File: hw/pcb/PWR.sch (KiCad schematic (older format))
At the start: 18 parts, among them J401 PWR, U401 R-78E3.3-1.0, U402 ADP7118

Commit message: wm8978 PCB design files
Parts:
- JP401: value Jumper_2_Open -> default open
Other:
- note added: "Bridge solder jumper if you do NOT want to use U402 (saves the expensive low noise \nLDO), however audio quality is significantly impacted by digital noise in my \nexperience. For pro audio quality U402 is mandatory!"
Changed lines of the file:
@@
 encoding utf-8
 Sheet 4 6
-Title "CTAG TBD Eurorack Audio Module"
-Date "2020-03-18"
-Rev "B"
+Title "CTAG-TBD"
+Date "2020-06-06"
+Rev "C"
 Comp "(c) Robert Manzke 2020"
 Comment1 "https://creativecommons.org/licenses/by-nc-sa/4.0/"
@@
 P 6900 2800
 F 0 "JP401" H 6900 3035 50  0000 C CNN
-F 1 "Jumper_2_Open" H 6900 2944 50  0000 C CNN
+F 1 "default open" H 6900 2944 50  0000 C CNN
 F 2 "Jumper:SolderJumper-2_P1.3mm_Open_TrianglePad1.0x1.5mm" H 6900 2800 50  0001 C CNN
 F 3 "~" H 6900 2800 50  0001 C CNN
@@
 Wire Wire Line
 	2800 2800 2800 2400
+Text Notes 6600 3250 0    50   ~ 0
+Bridge solder jumper if you do NOT want to use U402 (saves the expensive low noise \nLDO), however audio quality is significantly impacted by digital noise in my \nexperience. For pro audio quality U402 is mandatory!
 $EndSCHEMATC

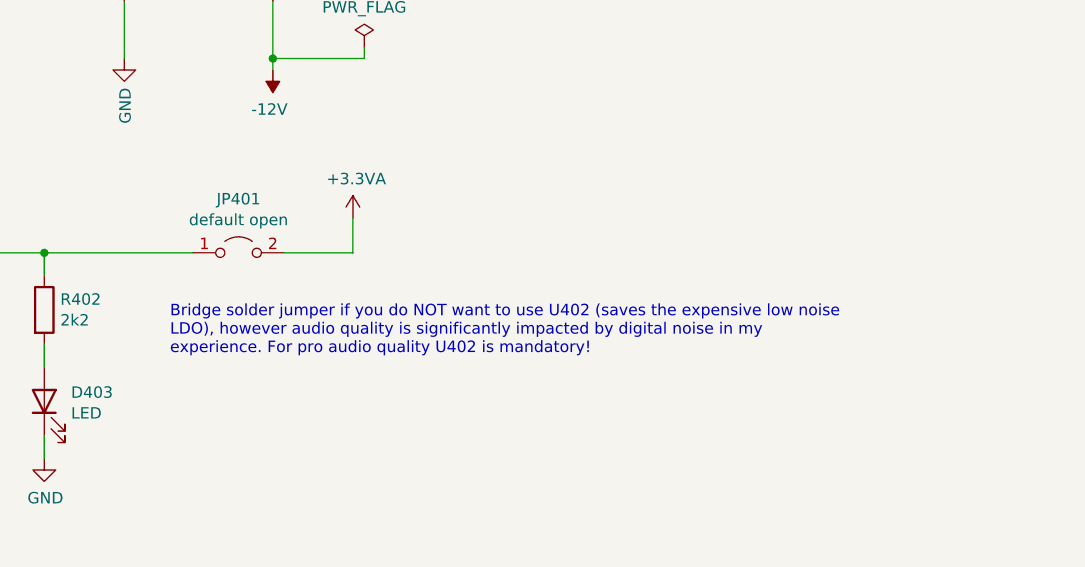
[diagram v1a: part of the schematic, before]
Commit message: fixed severe PCB issue, clearance of ground fills was too small, could lead to thermal instability
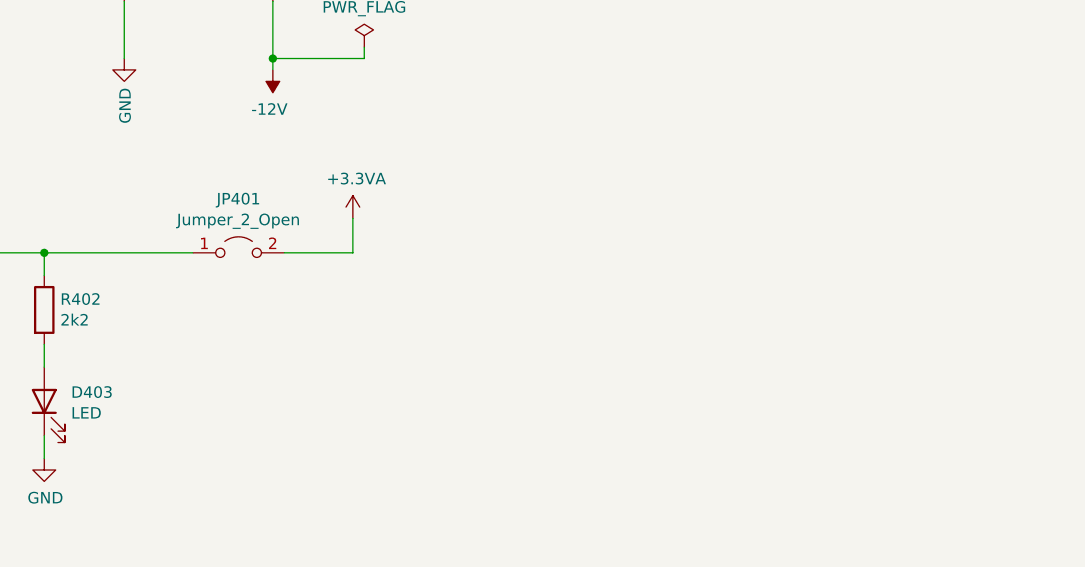
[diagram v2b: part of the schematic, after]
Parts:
- JP401: value default open -> Jumper_2_Open
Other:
- note removed: "Bridge solder jumper if you do NOT want to use U402 (saves the expensive low noise \nLDO), however audio quality is significantly impacted by digital noise in my \nexperience. For pro audio quality U402 is mandatory!"
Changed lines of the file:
@@
 encoding utf-8
 Sheet 4 6
-Title "CTAG-TBD"
-Date "2020-06-06"
-Rev "C"
+Title "ESP32 Eurorack Audio Module"
+Date "2020-08-18"
+Rev "G"
 Comp "(c) Robert Manzke 2020"
 Comment1 "https://creativecommons.org/licenses/by-nc-sa/4.0/"
@@
 P 6900 2800
 F 0 "JP401" H 6900 3035 50  0000 C CNN
-F 1 "default open" H 6900 2944 50  0000 C CNN
+F 1 "Jumper_2_Open" H 6900 2944 50  0000 C CNN
 F 2 "Jumper:SolderJumper-2_P1.3mm_Open_TrianglePad1.0x1.5mm" H 6900 2800 50  0001 C CNN
 F 3 "~" H 6900 2800 50  0001 C CNN
@@
 Wire Wire Line
 	2800 2800 2800 2400
-Text Notes 6600 3250 0    50   ~ 0
-Bridge solder jumper if you do NOT want to use U402 (saves the expensive low noise \nLDO), however audio quality is significantly impacted by digital noise in my \nexperience. For pro audio quality U402 is mandatory!
 $EndSCHEMATC

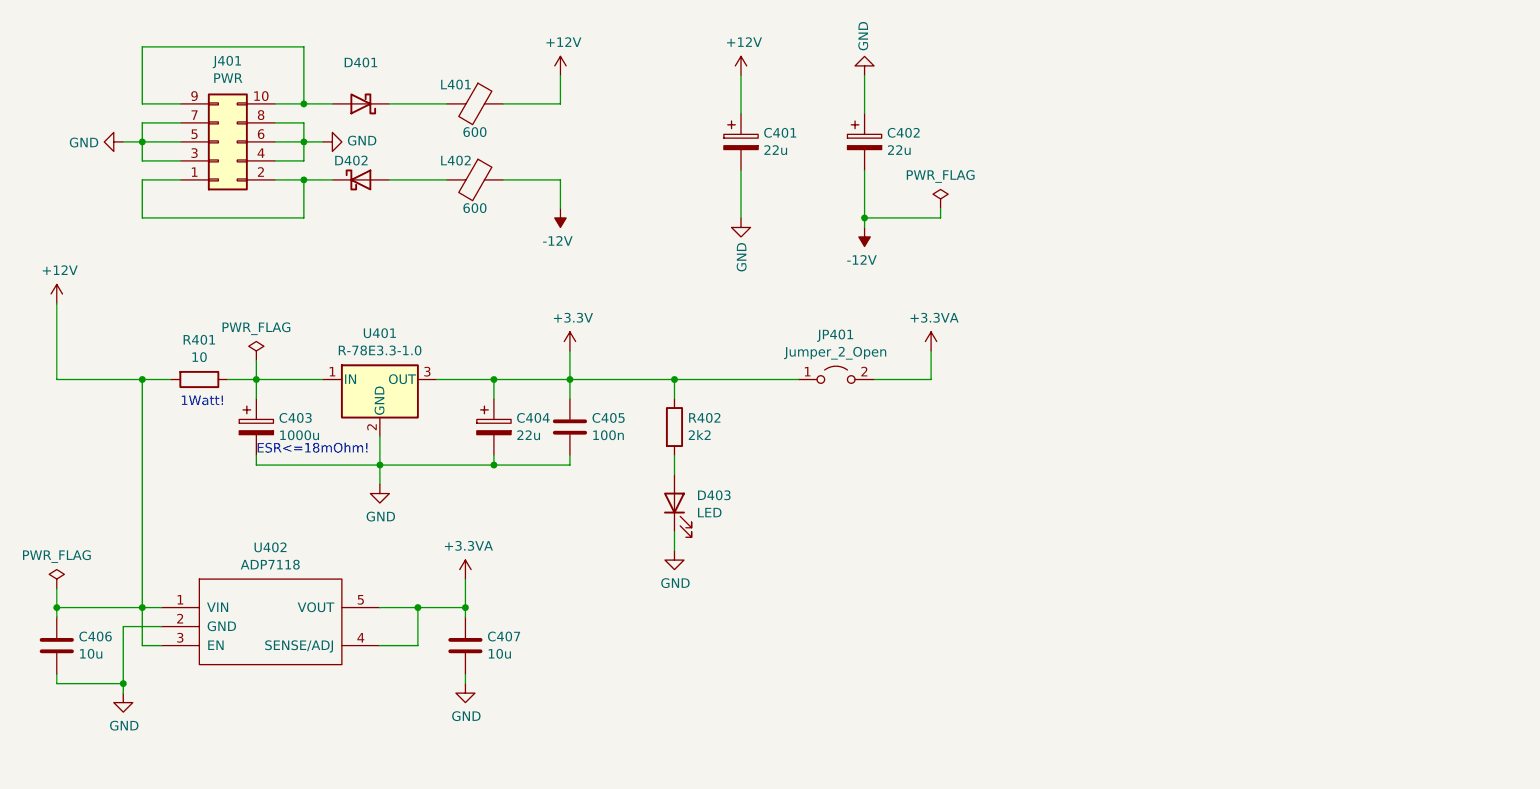
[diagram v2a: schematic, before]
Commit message: Updated Eurorack hw to Rev. H
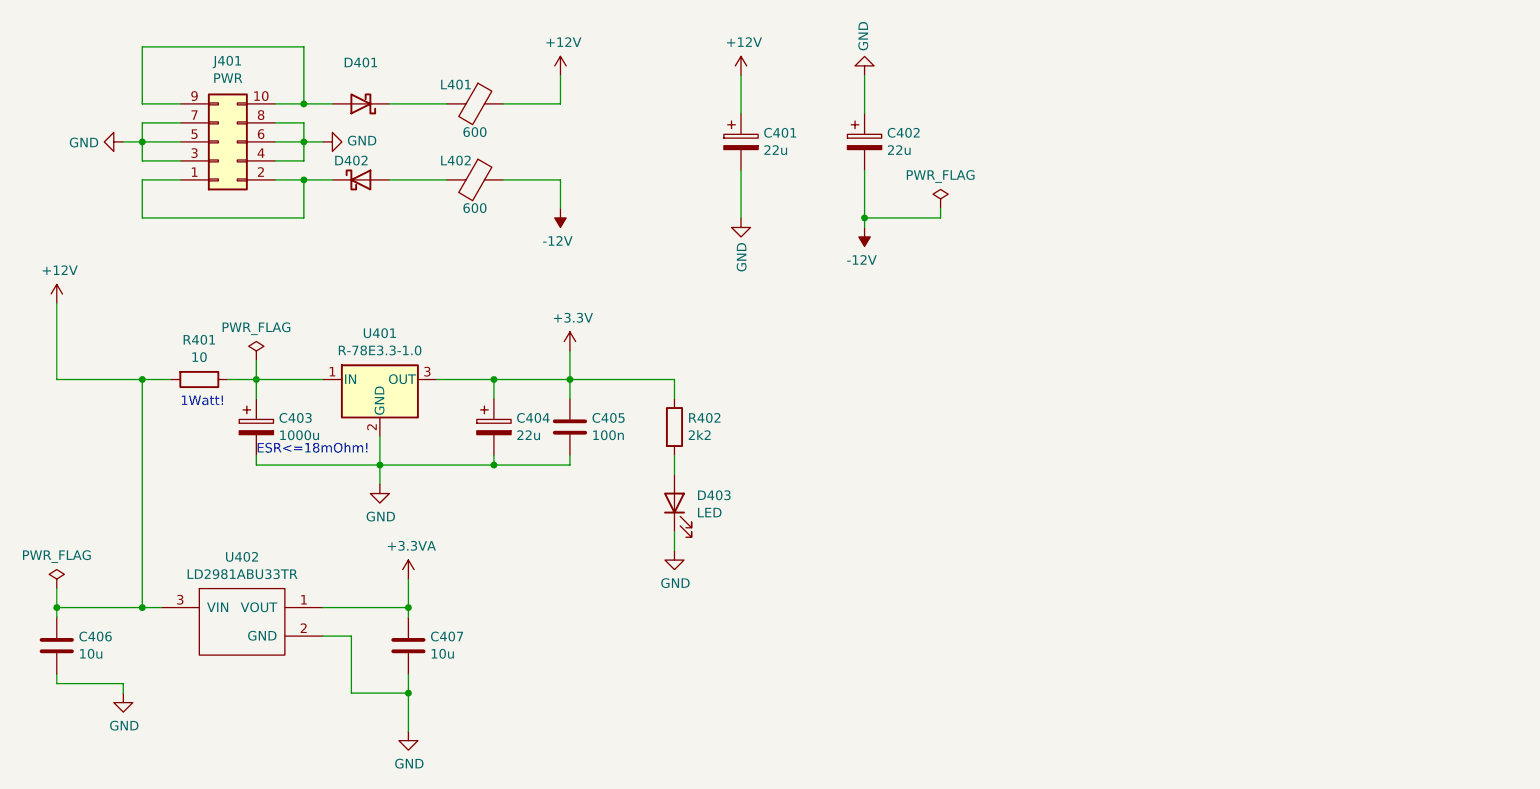
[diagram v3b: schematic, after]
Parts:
- removed JP401: Jumper_2_Open, Jumper:SolderJumper-2_P1.3mm_Open_TrianglePad1.0x1.5mm, symbol Jumper:Jumper_2_Open
- removed U402: ADP7118, Package_TO_SOT_SMD:TSOT-23-5, symbol ESP32-Eurorack-Audio-rescue:ADP7118-user
- added U402: LD2981ABU33TR, Package_TO_SOT_SMD:SOT-89-3, symbol special-ics:LD2981
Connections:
- net +12V: now also U402.3 (VIN)
- net +3.3VA: now also U402.1 (VOUT)
- net GND: now also U402.2 (GND)
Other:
- moved on the sheet: C407
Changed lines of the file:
@@
 Sheet 4 6
 Title "ESP32 Eurorack Audio Module"
-Date "2020-08-18"
-Rev "G"
-Comp "(c) Robert Manzke 2020"
+Date "2021-10-05"
+Rev "H"
+Comp "(c) Robert Manzke 2021"
 Comment1 "https://creativecommons.org/licenses/by-nc-sa/4.0/"
 Comment2 "Licensed under CC BY-NC-SA 4.0"
@@
 $EndComp
 Wire Wire Line
-	4700 4000 4500 4000
-Wire Wire Line
-	4700 4200 4700 4000
-Wire Wire Line
-	4500 4200 4700 4200
-Wire Wire Line
-	4950 4350 4950 4400
+	4650 4350 4650 4450
 $Comp
 L power:GND #PWR0415
 U 1 1 5B690874
-P 4950 4400
-F 0 "#PWR0415" H 4950 4150 50  0001 C CNN
-F 1 "GND" H 4955 4227 50  0000 C CNN
-F 2 "" H 4950 4400 50  0001 C CNN
-F 3 "" H 4950 4400 50  0001 C CNN
-	1    4950 4400
-	1    0    0    -1
-$EndComp
-Wire Wire Line
-	4950 4000 4950 4050
+P 4650 4650
+F 0 "#PWR0415" H 4650 4400 50  0001 C CNN
+F 1 "GND" H 4655 4477 50  0000 C CNN
+F 2 "" H 4650 4650 50  0001 C CNN
+F 3 "" H 4650 4650 50  0001 C CNN
+	1    4650 4650
+	1    0    0    -1
+$EndComp
+Wire Wire Line
+	4650 4000 4650 4050
 $Comp
 L Device:C C407
 U 1 1 5B68F2EB
-P 4950 4200
-F 0 "C407" H 5065 4246 50  0000 L CNN
-F 1 "10u" H 5065 4155 50  0000 L CNN
-F 2 "Capacitor_SMD:C_0402_1005Metric" H 4988 4050 50  0001 C CNN
-F 3 "~" H 4950 4200 50  0001 C CNN
-	1    4950 4200
+P 4650 4200
+F 0 "C407" H 4765 4246 50  0000 L CNN
+F 1 "10u" H 4765 4155 50  0000 L CNN
+F 2 "Capacitor_SMD:C_0402_1005Metric" H 4688 4050 50  0001 C CNN
+F 3 "~" H 4650 4200 50  0001 C CNN
+	1    4650 4200
 	1    0    0    -1
 $EndComp
@@
 	1    0    0    -1
 $EndComp
-Connection ~ 3150 4400
-Wire Wire Line
-	3150 4100 3150 4400
-Wire Wire Line
-	3350 4100 3150 4100
 $Comp
 L power:GND #PWR0416
@@
 	1    0    0    -1
 $EndComp
-Wire Wire Line
-	3250 4200 3250 4000
-Wire Wire Line
-	3350 4200 3250 4200
 Connection ~ 3250 4000
 Wire Wire Line
 	3350 4000 3250 4000
-Connection ~ 4700 4000
-Wire Wire Line
-	4950 4000 4700 4000
-$Comp
-L ESP32-Eurorack-Audio-rescue:ADP7118-user U?
-U 1 1 5B683013
-P 3550 4000
-AR Path="/5B683013" Ref="U?"  Part="1"
-AR Path="/5B69D53C/5B683013" Ref="U402"  Part="1"
-F 0 "U402" H 3925 4315 50  0000 C CNN
-F 1 "ADP7118" H 3925 4224 50  0000 C CNN
-F 2 "Package_TO_SOT_SMD:TSOT-23-5" H 3900 3650 50  0001 C CNN
-F 3 "" H 3550 4000 50  0001 C CNN
-	1    3550 4000
-	1    0    0    -1
-$EndComp
 Wire Wire Line
 	2800 2800 3250 2800
@@
 L power:+3.3VA #PWR0414
 U 1 1 5B6A656B
-P 4950 3850
-F 0 "#PWR0414" H 4950 3700 50  0001 C CNN
-F 1 "+3.3VA" H 4965 4023 50  0000 C CNN
-F 2 "" H 4950 3850 50  0001 C CNN
-F 3 "" H 4950 3850 50  0001 C CNN
-	1    4950 3850
-	1    0    0    -1
-$EndComp
-Connection ~ 4950 4000
-Wire Wire Line
-	4950 4000 4950 3850
-$Comp
-L Jumper:Jumper_2_Open JP401
-U 1 1 5DB17B7D
-P 6900 2800
-F 0 "JP401" H 6900 3035 50  0000 C CNN
-F 1 "Jumper_2_Open" H 6900 2944 50  0000 C CNN
-F 2 "Jumper:SolderJumper-2_P1.3mm_Open_TrianglePad1.0x1.5mm" H 6900 2800 50  0001 C CNN
-F 3 "~" H 6900 2800 50  0001 C CNN
-	1    6900 2800
-	1    0    0    -1
-$EndComp
+P 4650 3850
+F 0 "#PWR0414" H 4650 3700 50  0001 C CNN
+F 1 "+3.3VA" H 4665 4023 50  0000 C CNN
+F 2 "" H 4650 3850 50  0001 C CNN
+F 3 "" H 4650 3850 50  0001 C CNN
+	1    4650 3850
+	1    0    0    -1
+$EndComp
+Connection ~ 4650 4000
+Wire Wire Line
+	4650 4000 4650 3850
 Wire Wire Line
 	5500 2800 6050 2800
-Wire Wire Line
-	7100 2800 7400 2800
-Wire Wire Line
-	7400 2800 7400 2650
-$Comp
-L power:+3.3VA #PWR0411
-U 1 1 5DB1D1D7
-P 7400 2650
-F 0 "#PWR0411" H 7400 2500 50  0001 C CNN
-F 1 "+3.3VA" H 7415 2823 50  0000 C CNN
-F 2 "" H 7400 2650 50  0001 C CNN
-F 3 "" H 7400 2650 50  0001 C CNN
-	1    7400 2650
-	1    0    0    -1
-$EndComp
 $Comp
 L Device:R R402
@@
 Wire Wire Line
 	6050 2800 6050 2900
-Connection ~ 6050 2800
-Wire Wire Line
-	6050 2800 6700 2800
 $Comp
 L Device:LED D403
@@
 Wire Wire Line
 	2800 2800 2800 2400
+Wire Wire Line
+	4200 4000 4650 4000
+$Comp
+L special-ics:LD2981 U402
+U 1 1 615BEFE7
+P 3550 3900
+F 0 "U402" H 3775 4065 50  0000 C CNN
+F 1 "LD2981ABU33TR" H 3775 3974 50  0000 C CNN
+F 2 "Package_TO_SOT_SMD:SOT-89-3" H 3550 3900 50  0001 C CNN
+F 3 "" H 3550 3900 50  0001 C CNN
+	1    3550 3900
+	1    0    0    -1
+$EndComp
+Wire Wire Line
+	4200 4150 4350 4150
+Wire Wire Line
+	4350 4150 4350 4450
+Wire Wire Line
+	4350 4450 4650 4450
+Connection ~ 4650 4450
+Wire Wire Line
+	4650 4450 4650 4650
 $EndSCHEMATC
